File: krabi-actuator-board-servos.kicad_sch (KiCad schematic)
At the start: 12 parts

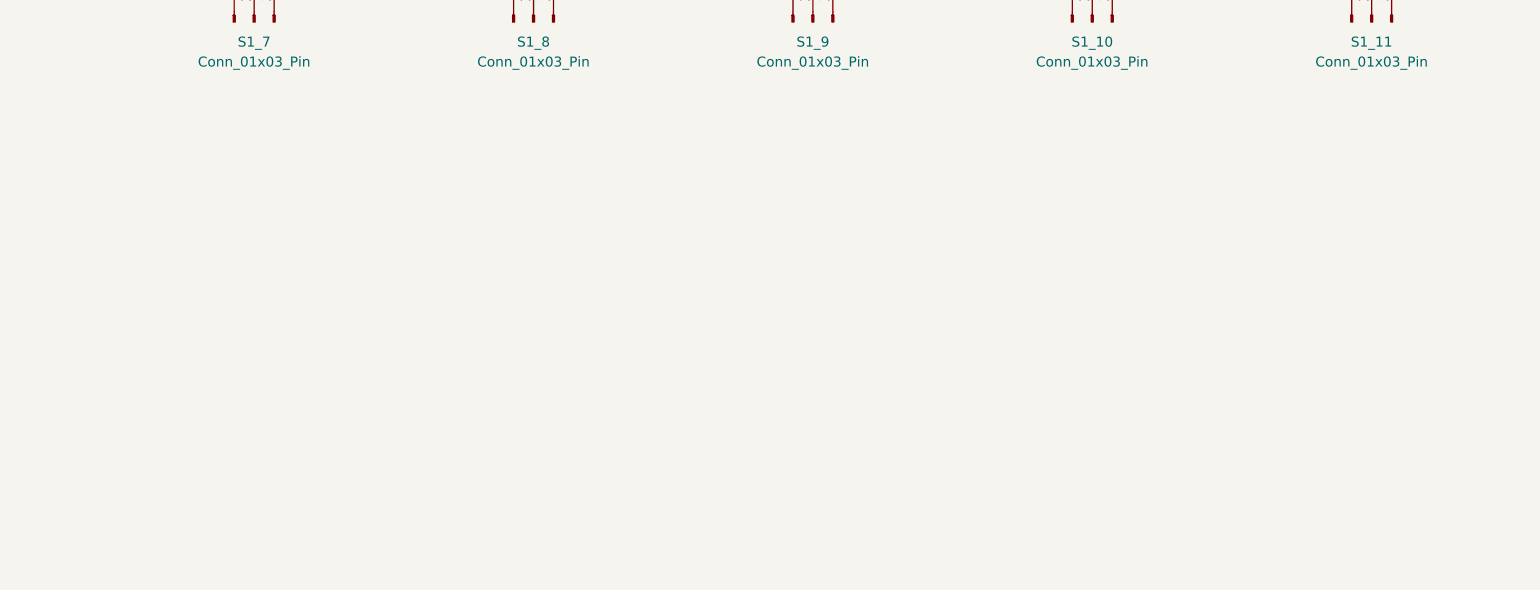
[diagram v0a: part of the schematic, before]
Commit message: Add Vaccum pump output and control
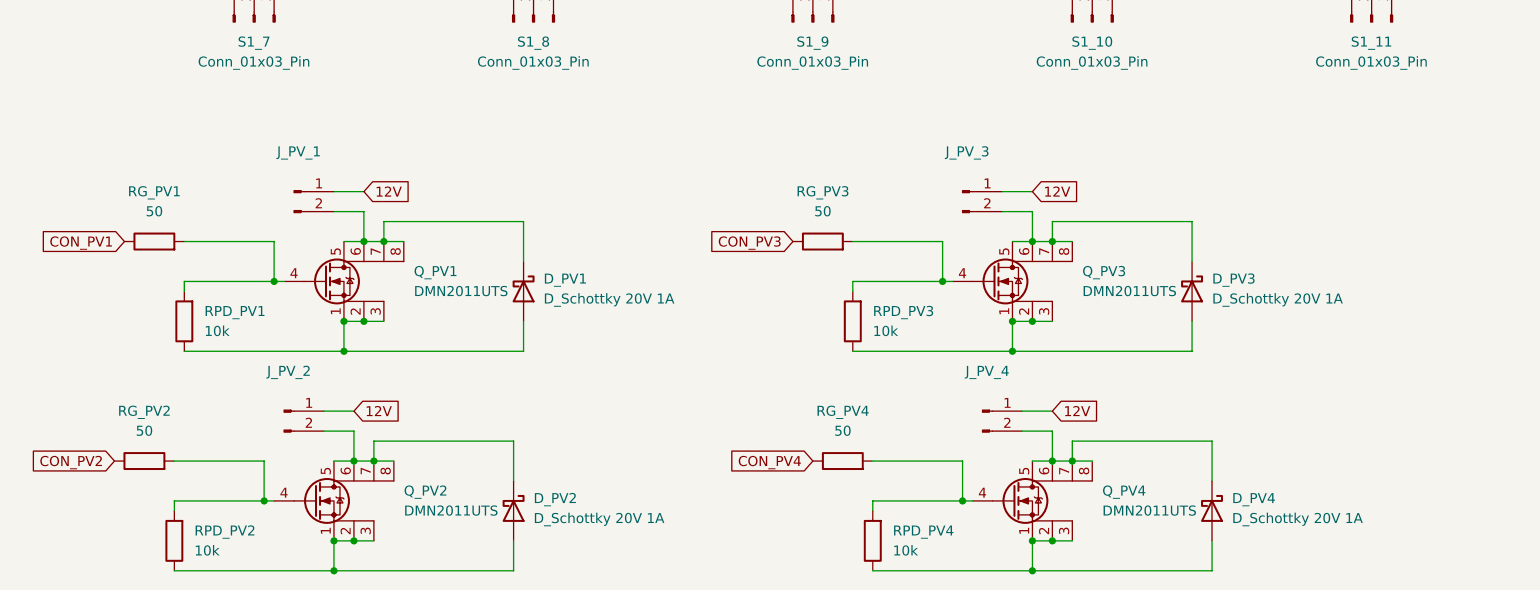
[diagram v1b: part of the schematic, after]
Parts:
- added D_PV1, D_PV2, D_PV3, D_PV4: D_Schottky 20V 1A, symbol Device:D_Schottky
- added J_PV_1, J_PV_2, J_PV_3, J_PV_4: ~, symbol Connector:Conn_01x02_Pin
- added Q_PV1, Q_PV2, Q_PV3, Q_PV4: DMN2011UTS, Package_SO:TSSOP-8_4.4x3mm_P0.65mm, symbol Krabi:DMN2011UTS
- added RG_PV1, RG_PV2, RG_PV3, RG_PV4: 50, symbol Device:R
- added RPD_PV1, RPD_PV2, RPD_PV3, RPD_PV4: 10k, symbol Device:R
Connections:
- new net: D_PV3.1 (K), J_PV_3.2 (Pin_2), Q_PV3.5 (D), Q_PV3.6 (D), Q_PV3.7 (D), Q_PV3.8 (D)
- new net: D_PV3.2 (A), Q_PV3.1 (S), Q_PV3.2 (S), Q_PV3.3 (S), RPD_PV3.1
- new net: D_PV4.1 (K), J_PV_4.2 (Pin_2), Q_PV4.5 (D), Q_PV4.6 (D), Q_PV4.7 (D), Q_PV4.8 (D)
- new net: D_PV1.2 (A), Q_PV1.1 (S), Q_PV1.2 (S), Q_PV1.3 (S), RPD_PV1.1
- new net: Q_PV1.4 (G), RG_PV1.2, RPD_PV1.2
- new net: D_PV1.1 (K), J_PV_1.2 (Pin_2), Q_PV1.5 (D), Q_PV1.6 (D), Q_PV1.7 (D), Q_PV1.8 (D)
- new net: Q_PV2.4 (G), RG_PV2.2, RPD_PV2.2
- new net: D_PV2.2 (A), Q_PV2.1 (S), Q_PV2.2 (S), Q_PV2.3 (S), RPD_PV2.1
- new net: D_PV2.1 (K), J_PV_2.2 (Pin_2), Q_PV2.5 (D), Q_PV2.6 (D), Q_PV2.7 (D), Q_PV2.8 (D)
- new net: Q_PV3.4 (G), RG_PV3.2, RPD_PV3.2
- new net: D_PV4.2 (A), Q_PV4.1 (S), Q_PV4.2 (S), Q_PV4.3 (S), RPD_PV4.1
- new net: Q_PV4.4 (G), RG_PV4.2, RPD_PV4.2
- new net 12V: J_PV_1.1 (Pin_1), J_PV_2.1 (Pin_1), J_PV_3.1 (Pin_1), J_PV_4.1 (Pin_1)
- new net CON_PV1: RG_PV1.1
- new net CON_PV2: RG_PV2.1
- new net CON_PV3: RG_PV3.1
- new net CON_PV4: RG_PV4.1

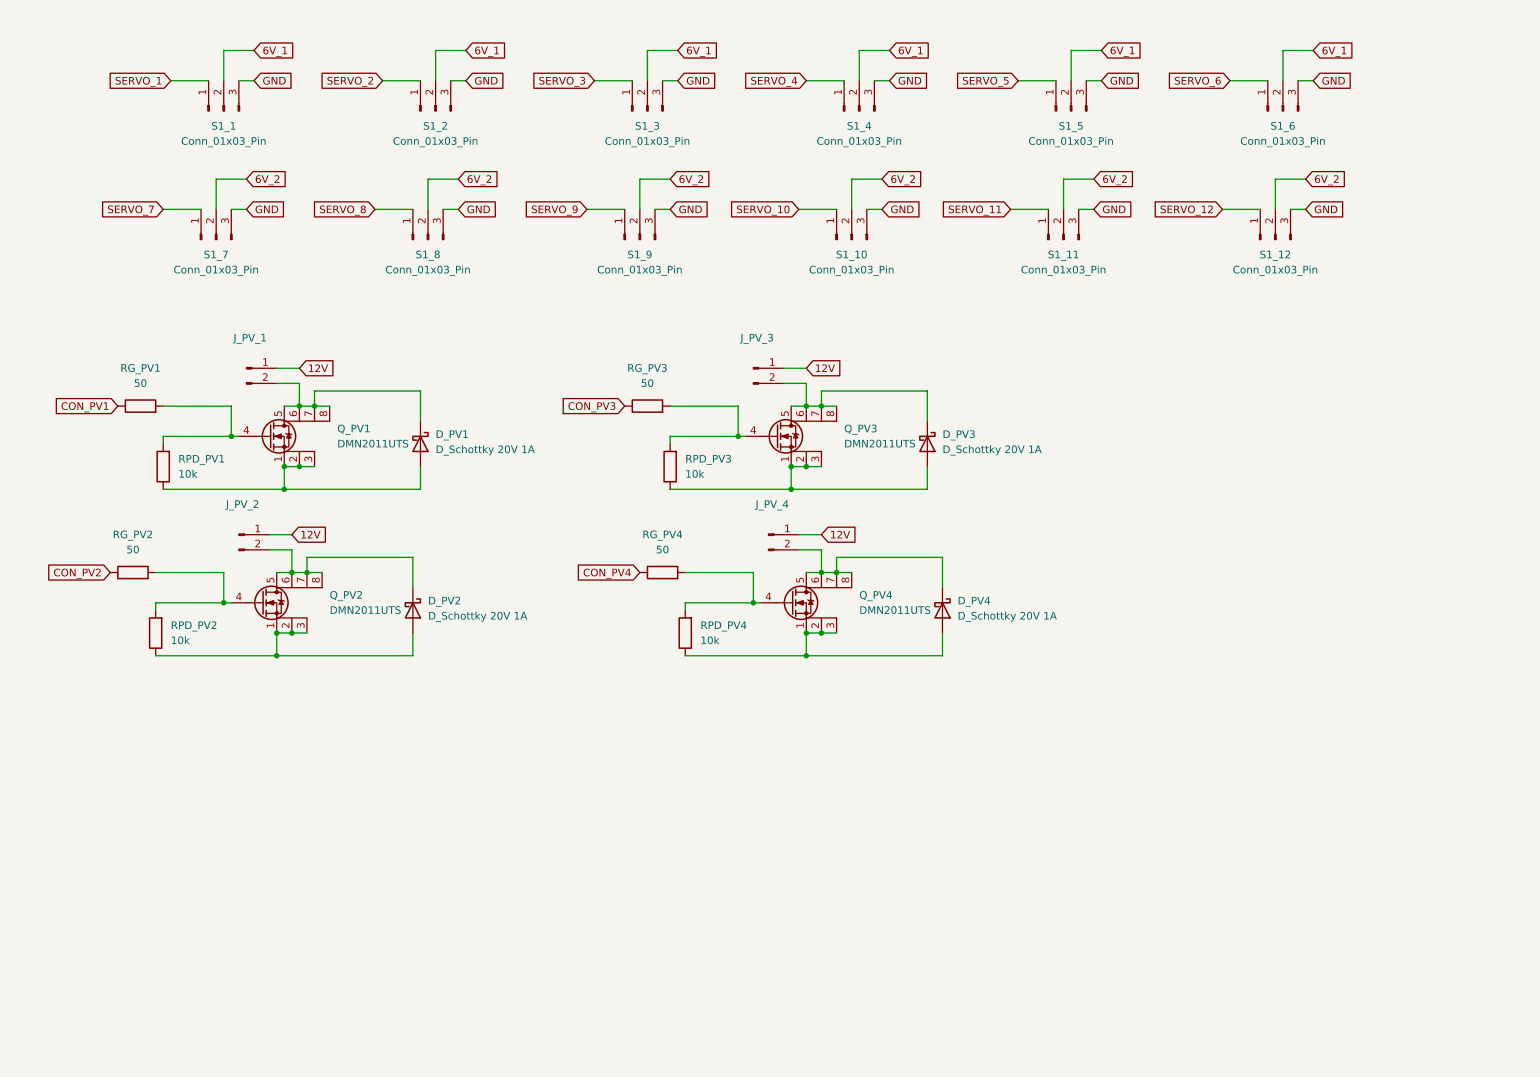
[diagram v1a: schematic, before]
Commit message: Measure the current of the Power supplies
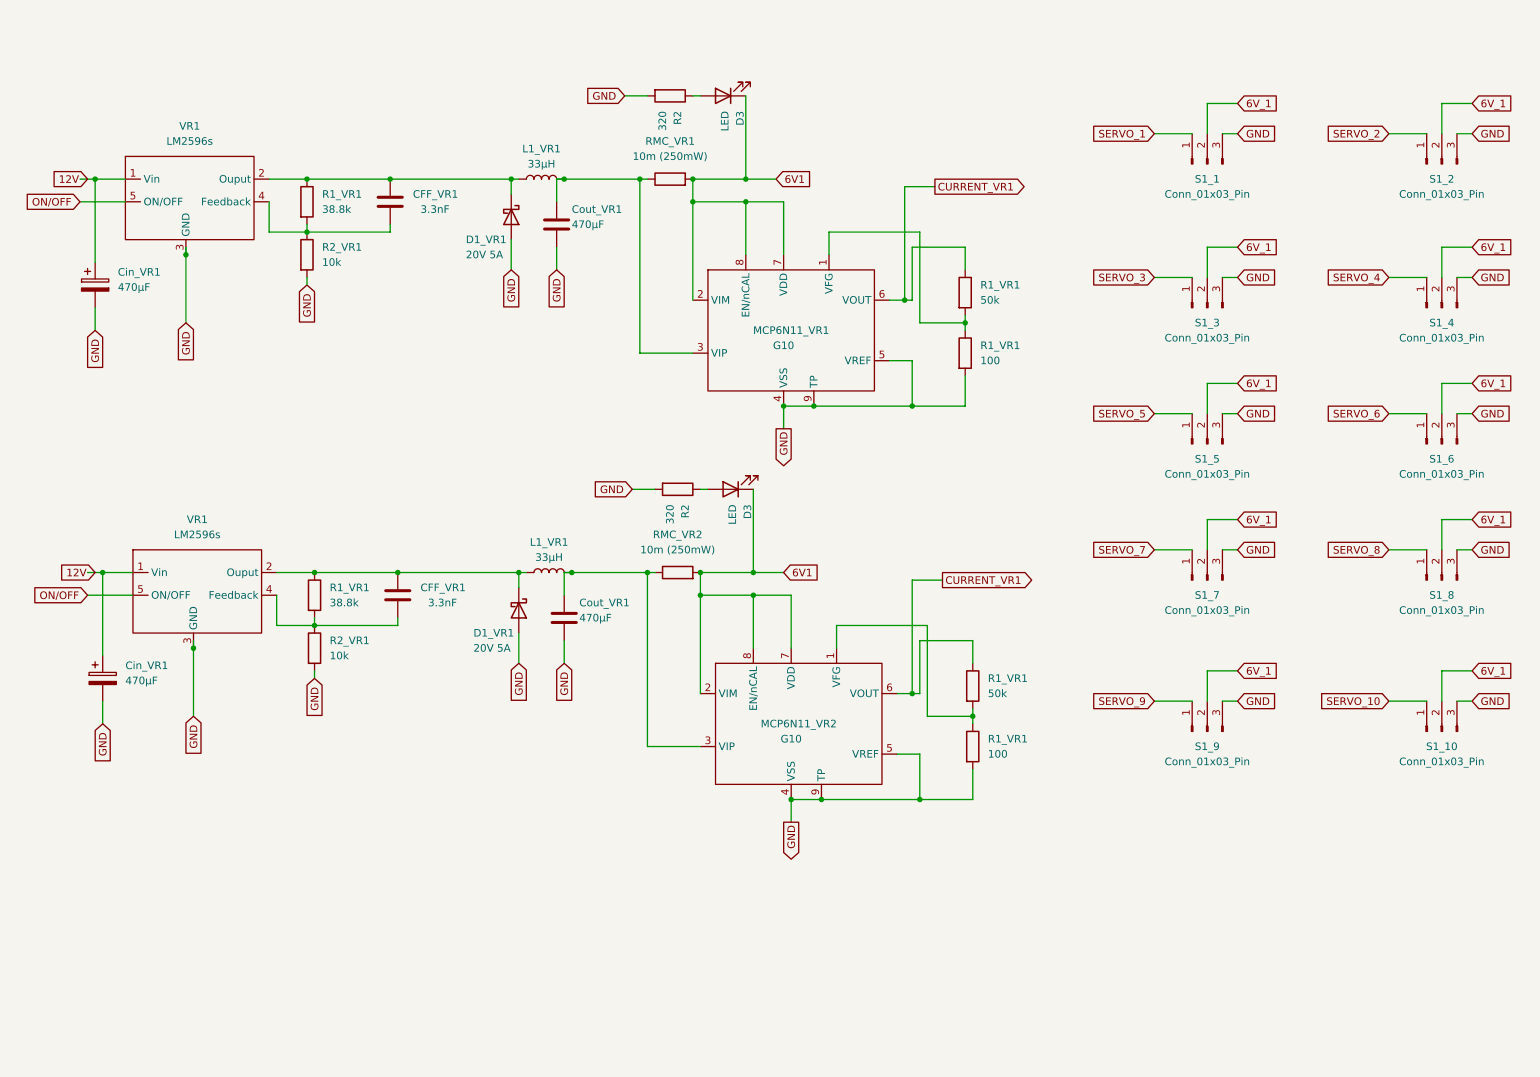
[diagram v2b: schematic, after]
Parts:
- removed D_PV1, D_PV2, D_PV3, D_PV4: D_Schottky 20V 1A, symbol Device:D_Schottky
- removed J_PV_1, J_PV_2, J_PV_3, J_PV_4: ~, symbol Connector:Conn_01x02_Pin
- removed Q_PV1, Q_PV2, Q_PV3, Q_PV4: DMN2011UTS, Package_SO:TSSOP-8_4.4x3mm_P0.65mm, symbol Krabi:DMN2011UTS
- removed RG_PV1, RG_PV2, RG_PV3, RG_PV4: 50, symbol Device:R
- removed RPD_PV1, RPD_PV2, RPD_PV3, RPD_PV4: 10k, symbol Device:R
- removed S1_11, S1_12: Conn_01x03_Pin, symbol Connector:Conn_01x03_Pin
- added CFF_VR1 (x2): 3.3nF, symbol Device:C
- added Cin_VR1 (x2): 470µF, Capacitor_THT:CP_Radial_D5.0mm_P2.00mm, symbol Device:C_Polarized
- added Cout_VR1 (x2): 470µF, symbol Device:C
- added D1_VR1 (x2): 20V 5A, Diode_SMD:D_0805_2012Metric, symbol Device:D_Schottky
- added D3 (x2): LED, LED_SMD:LED_0805_2012Metric, symbol Device:LED
- added L1_VR1 (x2): 33µH, symbol Device:L
- added MCP6N11_VR1, MCP6N11_VR2: G10, symbol Krabi:MCP611
- added R1_VR1 (x2): 38.8k, Resistor_SMD:R_0805_2012Metric, symbol Device:R
- added R1_VR1 (x2): 50k, Resistor_SMD:R_0805_2012Metric, symbol Device:R
- added R1_VR1 (x2): 100, Resistor_SMD:R_0805_2012Metric, symbol Device:R
- added R2 (x2): 320, Resistor_SMD:R_0805_2012Metric, symbol Device:R
- added R2_VR1 (x2): 10k, Resistor_SMD:R_0805_2012Metric, symbol Device:R
- added RMC_VR1, RMC_VR2: 10m (250mW), Resistor_SMD:R_1206_3216Metric, symbol Device:R
- added VR1 (x2): LM2596s, symbol Krabi:LM2596s
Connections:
- net 6V_2 is gone; now on net 6V_1: S1_10.2 (Pin_2), S1_7.2 (Pin_2), S1_8.2 (Pin_2), S1_9.2 (Pin_2)
- net 12V: now also Cin_VR1.1, Cin_VR1.1, VR1.1 (Vin), VR1.1 (Vin)
- net GND: now also Cin_VR1.2, Cin_VR1.2, Cout_VR1.2, Cout_VR1.2, D1_VR1.2 (A), D1_VR1.2 (A), MCP6N11_VR1.4 (VSS), MCP6N11_VR1.5 (VREF), MCP6N11_VR1.9 (TP), MCP6N11_VR2.4 (VSS), MCP6N11_VR2.5 (VREF), MCP6N11_VR2.9 (TP), R1_VR1.2, R1_VR1.2, R2.2, R2.2, R2_VR1.2, R2_VR1.2, VR1.3 (GND), VR1.3 (GND)
- new net: CFF_VR1.1, D1_VR1.1 (K), L1_VR1.1, R1_VR1.1, VR1.2 (Ouput) (x2)
- new net: CFF_VR1.2, R1_VR1.2, R2_VR1.1, VR1.4 (Feedback) (x2)
- new net: MCP6N11_VR1.1 (VFG), R1_VR1.1, R1_VR1.2
- new net: Cout_VR1.1, L1_VR1.2, MCP6N11_VR1.3 (VIP), RMC_VR1.1
- new net: Cout_VR1.1, L1_VR1.2, MCP6N11_VR2.3 (VIP), RMC_VR2.1
- new net: D3.2 (A), R2.1 (x2)
- new net: MCP6N11_VR2.1 (VFG), R1_VR1.1, R1_VR1.2
- new net 6V1: D3.1 (K), D3.1 (K), MCP6N11_VR1.2 (VIM), MCP6N11_VR1.7 (VDD), MCP6N11_VR1.8 (EN/nCAL), MCP6N11_VR2.2 (VIM), MCP6N11_VR2.7 (VDD), MCP6N11_VR2.8 (EN/nCAL), RMC_VR1.2, RMC_VR2.2
- new net CURRENT_VR1: MCP6N11_VR1.6 (VOUT), MCP6N11_VR2.6 (VOUT), R1_VR1.1, R1_VR1.1
- new net ON/OFF: VR1.5 (ON/OFF), VR1.5 (ON/OFF)
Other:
- moved on the sheet: S1_1

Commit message: Update servo with capa & add led strip page
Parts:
- removed S1_10, S1_2, S1_3, S1_4, S1_5, S1_6, S1_7, S1_8, S1_9: Conn_01x03_Pin, symbol Connector:Conn_01x03_Pin
- added C_SV1, C_SV10, C_SV11, C_SV12, C_SV2, C_SV3, C_SV4, C_SV5, C_SV6, C_SV7, C_SV8, C_SV9: 100nF, Capacitor_SMD:C_0805_2012Metric, symbol Device:C
- added SV10, SV11, SV12, SV2, SV3, SV4, SV5, SV6, SV7, SV8, SV9: Conn_01x03_Pin, symbol Connector:Conn_01x03_Pin
- renumbered S1_1 to SV1
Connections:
- net 6V1: no longer D3.1 (K), MCP6N11_VR2.2 (VIM), MCP6N11_VR2.7 (VDD), MCP6N11_VR2.8 (EN/nCAL), RMC_VR2.2
- net 6V_1: now also C_SV1.1, C_SV2.1, C_SV3.1, C_SV4.1, C_SV5.1, C_SV6.1, SV2.2 (Pin_2), SV3.2 (Pin_2), SV4.2 (Pin_2), SV5.2 (Pin_2), SV6.2 (Pin_2)
- net CURRENT_VR1: no longer MCP6N11_VR2.6 (VOUT), R1_VR1.1
- net GND: now also C_SV1.2, C_SV10.2, C_SV11.2, C_SV12.2, C_SV2.2, C_SV3.2, C_SV4.2, C_SV5.2, C_SV6.2, C_SV7.2, C_SV8.2, C_SV9.2, SV10.3 (Pin_3), SV11.3 (Pin_3), SV12.3 (Pin_3), SV2.3 (Pin_3), SV3.3 (Pin_3), SV4.3 (Pin_3), SV5.3 (Pin_3), SV6.3 (Pin_3), SV7.3 (Pin_3), SV8.3 (Pin_3), SV9.3 (Pin_3)
- net SERVO_10: now also SV10.1 (Pin_1)
- net SERVO_2: now also SV2.1 (Pin_1)
- net SERVO_3: now also SV3.1 (Pin_1)
- net SERVO_4: now also SV4.1 (Pin_1)
- net SERVO_5: now also SV5.1 (Pin_1)
- net SERVO_6: now also SV6.1 (Pin_1)
- net SERVO_7: now also SV7.1 (Pin_1)
- net SERVO_8: now also SV8.1 (Pin_1)
- net SERVO_9: now also SV9.1 (Pin_1)
- new net 6V2: D3.1 (K), MCP6N11_VR2.2 (VIM), MCP6N11_VR2.7 (VDD), MCP6N11_VR2.8 (EN/nCAL), RMC_VR2.2
- new net 6V_2: C_SV10.1, C_SV11.1, C_SV12.1, C_SV7.1, C_SV8.1, C_SV9.1, SV10.2 (Pin_2), SV11.2 (Pin_2), SV12.2 (Pin_2), SV7.2 (Pin_2), SV8.2 (Pin_2), SV9.2 (Pin_2)
- new net CURRENT_VR2: MCP6N11_VR2.6 (VOUT), R1_VR1.1
- new net SERVO_11: SV11.1 (Pin_1)
- new net SERVO_12: SV12.1 (Pin_1)
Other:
- moved on the sheet: SV1

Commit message: Assigning footprints to schemas
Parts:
- CFF_VR1: footprint (none) -> Capacitor_SMD:C_0805_2012Metric
- Cout_VR1: footprint (none) -> Capacitor_THT:CP_Radial_D13.0mm_P5.00mm
- L1_VR1: footprint (none) -> Krabi:BOURSPM5022
- MCP6N11_VR1, MCP6N11_VR2: footprint (none) -> Krabi:SOIC-8-1.27x5.4m
- SV1, SV10, SV11, SV12, SV2, SV3, SV4, SV5, SV6, SV7, SV8, SV9: footprint (none) -> Connector_PinSocket_2.54mm:PinSocket_1x03_P2.54mm_Vertical
- VR1: footprint (none) -> Package_TO_SOT_SMD:TO-263-5_TabPin6
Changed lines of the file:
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@@
       (effects (font (size 1.27 1.27)))
     )
-    (property "Footprint" "" (at 210.82 33.02 0)
+    (property "Footprint" "Connector_PinSocket_2.54mm:PinSocket_1x03_P2.54mm_Vertical" (at 210.82 33.02 0)
       (effects (font (size 1.27 1.27)) hide)
     )
@@
       (effects (font (size 1.27 1.27)))
     )
-    (property "Footprint" "" (at 137.16 50.8 0)
+    (property "Footprint" "Krabi:SOIC-8-1.27x5.4m" (at 137.16 50.8 0)
       (effects (font (size 1.27 1.27)) hide)
     )
@@
       (effects (font (size 1.27 1.27)))
     )
-    (property "Footprint" "" (at 246.38 60.96 0)
+    (property "Footprint" "Connector_PinSocket_2.54mm:PinSocket_1x03_P2.54mm_Vertical" (at 246.38 60.96 0)
       (effects (font (size 1.27 1.27)) hide)
     )
@@
       (effects (font (size 1.27 1.27)))
     )
-    (property "Footprint" "" (at 246.38 113.03 0)
+    (property "Footprint" "Connector_PinSocket_2.54mm:PinSocket_1x03_P2.54mm_Vertical" (at 246.38 113.03 0)
       (effects (font (size 1.27 1.27)) hide)
     )
@@
       (effects (font (size 1.27 1.27)) (justify left))
     )
-    (property "Footprint" "" (at 73.3552 115.57 0)
+    (property "Footprint" "Capacitor_SMD:C_0805_2012Metric" (at 73.3552 115.57 0)
       (effects (font (size 1.27 1.27)) hide)
     )
@@
       (effects (font (size 1.27 1.27)))
     )
-    (property "Footprint" "" (at 209.55 142.24 0)
+    (property "Footprint" "Connector_PinSocket_2.54mm:PinSocket_1x03_P2.54mm_Vertical" (at 209.55 142.24 0)
       (effects (font (size 1.27 1.27)) hide)
     )
@@
       (effects (font (size 1.27 1.27)) (justify left))
     )
-    (property "Footprint" "" (at 72.0852 49.53 0)
+    (property "Footprint" "Capacitor_SMD:C_0805_2012Metric" (at 72.0852 49.53 0)
       (effects (font (size 1.27 1.27)) hide)
     )
@@
       (effects (font (size 1.27 1.27)))
     )
-    (property "Footprint" "" (at 246.38 87.63 0)
+    (property "Footprint" "Connector_PinSocket_2.54mm:PinSocket_1x03_P2.54mm_Vertical" (at 246.38 87.63 0)
       (effects (font (size 1.27 1.27)) hide)
     )
@@
       (effects (font (size 1.27 1.27)))
     )
-    (property "Footprint" "" (at 41.91 109.22 0)
+    (property "Footprint" "Package_TO_SOT_SMD:TO-263-5_TabPin6" (at 41.91 109.22 0)
       (effects (font (size 1.27 1.27)) hide)
     )
@@
       (effects (font (size 1.27 1.27)))
     )
-    (property "Footprint" "" (at 210.82 60.96 0)
+    (property "Footprint" "Connector_PinSocket_2.54mm:PinSocket_1x03_P2.54mm_Vertical" (at 210.82 60.96 0)
       (effects (font (size 1.27 1.27)) hide)
     )
@@
       (effects (font (size 1.27 1.27)))
     )
-    (property "Footprint" "" (at 138.43 116.84 0)
+    (property "Footprint" "Krabi:SOIC-8-1.27x5.4m" (at 138.43 116.84 0)
       (effects (font (size 1.27 1.27)) hide)
     )
@@
       (effects (font (size 1.27 1.27)))
     )
-    (property "Footprint" "" (at 40.64 43.18 0)
+    (property "Footprint" "Package_TO_SOT_SMD:TO-263-5_TabPin6" (at 40.64 43.18 0)
       (effects (font (size 1.27 1.27)) hide)
     )
@@
       (effects (font (size 1.27 1.27)))
     )
-    (property "Footprint" "" (at 210.82 87.63 0)
+    (property "Footprint" "Connector_PinSocket_2.54mm:PinSocket_1x03_P2.54mm_Vertical" (at 210.82 87.63 0)
       (effects (font (size 1.27 1.27)) hide)
     )
@@
       (effects (font (size 1.27 1.27)))
     )
-    (property "Footprint" "" (at 96.52 41.91 0)
+    (property "Footprint" "Krabi:BOURSPM5022" (at 96.52 41.91 0)
       (effects (font (size 1.27 1.27)) hide)
     )
@@
       (effects (font (size 1.27 1.27)) (justify left))
     )
-    (property "Footprint" "" (at 100.0252 53.34 0)
+    (property "Footprint" "Capacitor_THT:CP_Radial_D13.0mm_P5.00mm" (at 100.0252 53.34 0)
       (effects (font (size 1.27 1.27)) hide)
     )
@@
       (effects (font (size 1.27 1.27)) (justify left))
     )
-    (property "Footprint" "" (at 101.2952 119.38 0)
+    (property "Footprint" "Capacitor_THT:CP_Radial_D13.0mm_P5.00mm" (at 101.2952 119.38 0)
       (effects (font (size 1.27 1.27)) hide)
     )
@@
       (effects (font (size 1.27 1.27)))
     )
-    (property "Footprint" "" (at 97.79 107.95 0)
+    (property "Footprint" "Krabi:BOURSPM5022" (at 97.79 107.95 0)
       (effects (font (size 1.27 1.27)) hide)
     )
@@
       (effects (font (size 1.27 1.27)))
     )
-    (property "Footprint" "" (at 107.95 184.15 0)
+    (property "Footprint" "Connector_PinSocket_2.54mm:PinSocket_1x03_P2.54mm_Vertical" (at 107.95 184.15 0)
       (effects (font (size 1.27 1.27)) hide)
     )
@@
       (effects (font (size 1.27 1.27)))
     )
-    (property "Footprint" "" (at 246.38 33.02 0)
+    (property "Footprint" "Connector_PinSocket_2.54mm:PinSocket_1x03_P2.54mm_Vertical" (at 246.38 33.02 0)
       (effects (font (size 1.27 1.27)) hide)
     )
@@
       (effects (font (size 1.27 1.27)))
     )
-    (property "Footprint" "" (at 144.78 182.88 0)
+    (property "Footprint" "Connector_PinSocket_2.54mm:PinSocket_1x03_P2.54mm_Vertical" (at 144.78 182.88 0)
       (effects (font (size 1.27 1.27)) hide)
     )
@@
       (effects (font (size 1.27 1.27)))
     )
-    (property "Footprint" "" (at 246.38 140.97 0)
+    (property "Footprint" "Connector_PinSocket_2.54mm:PinSocket_1x03_P2.54mm_Vertical" (at 246.38 140.97 0)
       (effects (font (size 1.27 1.27)) hide)
     )
@@
       (effects (font (size 1.27 1.27)))
     )
-    (property "Footprint" "" (at 210.82 115.57 0)
-      (effects (font (size 1.27 1.27)) hide)
-    )
+    (property "Footprint" "Connector_PinSocket_2.54mm:PinSocket_1x03_P2.54mm_Vertical" (at 210.82 115.57 0)
+      (effects (font (size 1.27 1.27)) hide)
+    )
